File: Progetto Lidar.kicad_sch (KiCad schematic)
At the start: 18 parts, among them IC1 TLV74133PDBVR, J1 CONN_LASER, J2 Conn_Coaxial, Y1 SiT2024BA-S2-33E-8.000000G

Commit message: Finito lo schematico e aggiunto modelli 3D
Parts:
- removed C?: 0.1uF, symbol Device:C
- removed C?: 1uF, symbol Device:C
- added C3, C5, C6: 100nF, Capacitor_SMD:C_0805_2012Metric, symbol Device:C
- added J10, J5, J6, J7, J9: Conn_01x08, Connector_PinSocket_2.54mm:PinSocket_1x08_P2.54mm_Vertical, symbol Connector_Generic:Conn_01x08
- added J3: Conn_02x18_Odd_Even, Connector_PinSocket_2.54mm:PinSocket_2x18_P2.54mm_Vertical, symbol Connector_Generic:Conn_02x18_Odd_Even
- added J4: Conn_01x10, Connector_PinSocket_2.54mm:PinSocket_1x10_P2.54mm_Vertical, symbol Connector_Generic:Conn_01x10
- added J8: Conn_SPI, Connector_PinSocket_2.54mm:PinSocket_2x03_P2.54mm_Vertical, symbol Connector_Generic:Conn_02x03_Odd_Even
- C1: value C -> 0.1uF; footprint (none) -> Capacitor_SMD:C_0805_2012Metric
- C2: value C -> 1uF; footprint (none) -> Capacitor_SMD:C_0805_2012Metric
- C4: renamed from C?; footprint (none) -> Capacitor_SMD:C_0805_2012Metric
- C7: renamed from C?; value 1uF -> 100nF; footprint (none) -> Capacitor_SMD:C_0805_2012Metric
- J1, J2: footprint (none) -> Libreria_componenti_footprint:731713150
- JP1, JP3: renamed from JP?; footprint (none) -> Jumper:SolderJumper-2_P1.3mm_Open_RoundedPad1.0x1.5mm
- JP2: renamed from JP?; footprint (none) -> Jumper:SolderJumper-3_P1.3mm_Open_Pad1.0x1.5mm_NumberLabels
- R1: renamed from R?; footprint (none) -> Resistor_SMD:R_0805_2012Metric
- renumbered IC to IC2
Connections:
- net +3V3: now also C3.1, C5.1, C6.1; no longer IC_1.14 (VDD)
- net +5V: now also A1.5V2 (SPI_5V), A1.5V3 (5V), A1.5V4 (5V), J3.1 (Pin_1), J3.2 (Pin_2), J7.5 (Pin_5), J8.2 (Pin_2)
- net 3V3_ARDUINO: now also J7.4 (Pin_4)
- net ARD_BUFF_EN: now also J5.3 (Pin_3)
- net ARD_TRIG: now also J5.4 (Pin_4)
- net ARD_V_REF: now also J5.5 (Pin_5)
- net GND: now also A1.GND4 (SPI_GND), J1.MH1 (Ext), J2.MH1 (Ext), C5.2, C6.2, J3.35 (Pin_35), J3.36 (Pin_36), J4.4 (Pin_4), J7.6 (Pin_6), J7.7 (Pin_7), J8.6 (Pin_6); no longer J1.2 (Ext), J2.2 (Ext)
- net SPI_CS: now also J5.6 (Pin_6)
- net SPI_MISO: now also J8.1 (Pin_1)
- net SPI_MOSI: now also J8.4 (Pin_4)
- net SPI_SCK: now also J8.3 (Pin_3)
- net at C2.1, IC1.5 (OUT): now also JP2.1 (A)
- net ARD_AN_A0: now reaches A1.A0
- net ARD_AN_A0: now also J9.1 (Pin_1)
- net ARD_AN_A1: now reaches A1.A1
- net ARD_AN_A1: now also J9.2 (Pin_2)
- net ARD_AN_A10: now reaches A1.A10
- net ARD_AN_A10: now also J10.3 (Pin_3)
- net ARD_AN_A11: now reaches A1.A11
- net ARD_AN_A11: now also J10.4 (Pin_4)
- net ARD_AN_A2: now reaches A1.A2
- net ARD_AN_A2: now also J9.3 (Pin_3)
- net ARD_AN_A3: now reaches A1.A3
- net ARD_AN_A3: now also J9.4 (Pin_4)
- net ARD_AN_A4: now reaches A1.A4
- net ARD_AN_A4: now also J9.5 (Pin_5)
- net ARD_AN_A5: now reaches A1.A5
- net ARD_AN_A5: now also J9.6 (Pin_6)
- net ARD_AN_A6: now reaches A1.A6
- net ARD_AN_A6: now also J9.7 (Pin_7)
- net ARD_AN_A7: now reaches A1.A7
- net ARD_AN_A7: now also J9.8 (Pin_8)
- net ARD_AN_A8: now reaches A1.A8
- net ARD_AN_A8: now also J10.1 (Pin_1)
- net ARD_AN_A9: now reaches A1.A9
- net ARD_AN_A9: now also J10.2 (Pin_2)
- net ARD_AN_AREF: now reaches A1.AREF
- net ARD_AN_AREF: now also J4.3 (Pin_3)
- net ARD_CAN_RX: now reaches A1.CANR (CANRX)
- net ARD_CAN_RX: now also J10.7 (Pin_7)
- net ARD_CAN_TX: now reaches A1.CANT (CANTX)
- net ARD_CAN_TX: now also J10.8 (Pin_8)
- net ARD_SR_RX0: now reaches A1.D0 (D0/RX0)
- net ARD_SR_RX0: now also J5.8 (Pin_8)
- net ARD_SR_TX0: now reaches A1.D1 (D1/TX0)
- net ARD_SR_TX0: now also J5.7 (Pin_7)
- net ARD_GPIO_D10: now reaches A1.D10 (D10_CS0)
- net ARD_GPIO_D10: now also J4.8 (Pin_8)
- net ARD_GPIO_D11: now reaches A1.D11
- net ARD_GPIO_D11: now also J4.7 (Pin_7)
- net ARD_GPIO_D12: now reaches A1.D12
- net ARD_GPIO_D12: now also J4.6 (Pin_6)
- net ARD_GPIO_D13: now reaches A1.D13
- net ARD_GPIO_D13: now also J4.5 (Pin_5)
- net ARD_SR_TX3: now reaches A1.D14 (D14/TX3)
- net ARD_SR_TX3: now also J6.1 (Pin_1)
- net ARD_SR_RX3: now reaches A1.D15 (D15/RX3)
- net ARD_SR_RX3: now also J6.2 (Pin_2)
- net ARD_SR_TX2: now reaches A1.D16 (D16/TX2)
- net ARD_SR_TX2: now also J6.3 (Pin_3)
- net ARD_SR_RX2: now reaches A1.D17 (D17/RX2)
- net ARD_SR_RX2: now also J6.4 (Pin_4)
- net ARD_SR_TX1: now reaches A1.D18 (D18/TX1)
- net ARD_SR_TX1: now also J6.5 (Pin_5)
- net ARD_SR_RX1: now reaches A1.D19 (D19/RX1)
- net ARD_SR_RX1: now also J6.6 (Pin_6)
- net ARD_I2C_SDA: now reaches A1.D20 (D20/SDA)
- net ARD_I2C_SDA: now also J6.7 (Pin_7)
- net ARD_I2C_SCL: now reaches A1.D21 (D21/SCL)
- net ARD_I2C_SCL: now also J6.8 (Pin_8)
- net ARD_GPIO_D22: now reaches A1.D22
- net ARD_GPIO_D22: now also J3.3 (Pin_3)
- net ARD_GPIO_D23: now reaches A1.D23
- net ARD_GPIO_D23: now also J3.4 (Pin_4)
- net ARD_GPIO_D24: now reaches A1.D24
- net ARD_GPIO_D24: now also J3.5 (Pin_5)
- net ARD_GPIO_D25: now reaches A1.D25
- net ARD_GPIO_D25: now also J3.6 (Pin_6)
- net ARD_GPIO_D26: now reaches A1.D26
- net ARD_GPIO_D26: now also J3.7 (Pin_7)
- net ARD_GPIO_D27: now reaches A1.D27
- net ARD_GPIO_D27: now also J3.8 (Pin_8)
- net ARD_GPIO_D28: now reaches A1.D28
- net ARD_GPIO_D28: now also J3.9 (Pin_9)
- net ARD_GPIO_D29: now reaches A1.D29
- net ARD_GPIO_D29: now also J3.10 (Pin_10)
- net ARD_GPIO_D30: now reaches A1.D30
- net ARD_GPIO_D30: now also J3.11 (Pin_11)
- net ARD_GPIO_D31: now reaches A1.D31
- net ARD_GPIO_D31: now also J3.12 (Pin_12)
- net ARD_GPIO_D32: now reaches A1.D32
- net ARD_GPIO_D32: now also J3.13 (Pin_13)
- net ARD_GPIO_D33: now reaches A1.D33
- net ARD_GPIO_D33: now also J3.14 (Pin_14)
- net ARD_GPIO_D34: now reaches A1.D34
- net ARD_GPIO_D34: now also J3.15 (Pin_15)
- net ARD_GPIO_D35: now reaches A1.D35
- net ARD_GPIO_D35: now also J3.16 (Pin_16)
- net ARD_GPIO_D36: now reaches A1.D36
- net ARD_GPIO_D36: now also J3.17 (Pin_17)
- net ARD_GPIO_D37: now reaches A1.D37
- net ARD_GPIO_D37: now also J3.18 (Pin_18)
- net ARD_GPIO_D38: now reaches A1.D38
- net ARD_GPIO_D38: now also J3.19 (Pin_19)
- net ARD_GPIO_D39: now reaches A1.D39
- net ARD_GPIO_D39: now also J3.20 (Pin_20)
- net ARD_GPIO_D40: now reaches A1.D40
- net ARD_GPIO_D40: now also J3.21 (Pin_21)
- net ARD_GPIO_D41: now reaches A1.D41
- net ARD_GPIO_D41: now also J3.22 (Pin_22)
- net ARD_GPIO_D42: now reaches A1.D42
- net ARD_GPIO_D42: now also J3.23 (Pin_23)
- net ARD_GPIO_D43: now reaches A1.D43
- net ARD_GPIO_D43: now also J3.24 (Pin_24)
- net ARD_GPIO_D44: now reaches A1.D44
- net ARD_GPIO_D44: now also J3.25 (Pin_25)
- net ARD_GPIO_45: now reaches A1.D45
- net ARD_GPIO_45: now also J3.26 (Pin_26)
- net ARD_GPIO_46: now reaches A1.D46
- net ARD_GPIO_46: now also J3.27 (Pin_27)
- net ARD_GPIO_47: now reaches A1.D47
- net ARD_GPIO_47: now also J3.28 (Pin_28)
- net ARD_GPIO_48: now reaches A1.D48
- net ARD_GPIO_48: now also J3.29 (Pin_29)
- net ARD_GPIO_49: now reaches A1.D49
- net ARD_GPIO_49: now also J3.30 (Pin_30)
- net ARD_GPIO_50: now reaches A1.D50
- net ARD_GPIO_50: now also J3.31 (Pin_31)
- net ARD_GPIO_51: now reaches A1.D51
- net ARD_GPIO_51: now also J3.32 (Pin_32)
- net ARD_GPIO_52: now reaches A1.D52 (D52_CS2)
- net ARD_GPIO_52: now also J3.33 (Pin_33)
- net ARD_GPIO_D53: now reaches A1.D53
- net ARD_GPIO_D53: now also J3.34 (Pin_34)
- net ARD_GPIO_D6: now reaches A1.D6
- net ARD_GPIO_D6: now also J5.2 (Pin_2)
- net ARD_GPIO_D7: now reaches A1.D7
- net ARD_GPIO_D7: now also J5.1 (Pin_1)
- net ARD_GPIO_D8: now reaches A1.D8
- net ARD_GPIO_D8: now also J4.10 (Pin_10)
- net ARD_GPIO_D9: now reaches A1.D9
- net ARD_GPIO_D9: now also J4.9 (Pin_9)
- net ARD_AN_DAC0: now reaches A1.DAC0
- net ARD_AN_DAC0: now also J10.5 (Pin_5)
- net ARD_AN_DAC1: now reaches A1.DAC1
- net ARD_AN_DAC1: now also J10.6 (Pin_6)
- net ARD_AN_IORF: now reaches A1.IORF (IOREF)
- net ARD_AN_IORF: now also J7.2 (Pin_2)
- net ARD_AN_RST1: now reaches A1.RST1 (RESET)
- net ARD_AN_RST1: now also J7.3 (Pin_3)
- net SPI_RESET: now reaches A1.RST2 (SPI_RESET)
- net SPI_RESET: now also J8.5 (Pin_5)
- net ARD_I2C_SCL1: now reaches A1.SCL1
- net ARD_I2C_SCL1: now also J4.1 (Pin_1)
- net ARD_I2C_SDA1: now reaches A1.SDA1
- net ARD_I2C_SDA1: now also J4.2 (Pin_2)
- net ARD_VIN: now reaches A1.VIN
- net ARD_VIN: now also J7.8 (Pin_8)
- new net: C3.2, IC_1.14 (VDD)
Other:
- note added: "Ceramico con ESR: 100 mOhm max"
- moved on the sheet: A1, C1, C2, C4, C7, IC1, IC2, IC_1, IC_2, J1, J2, JP1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

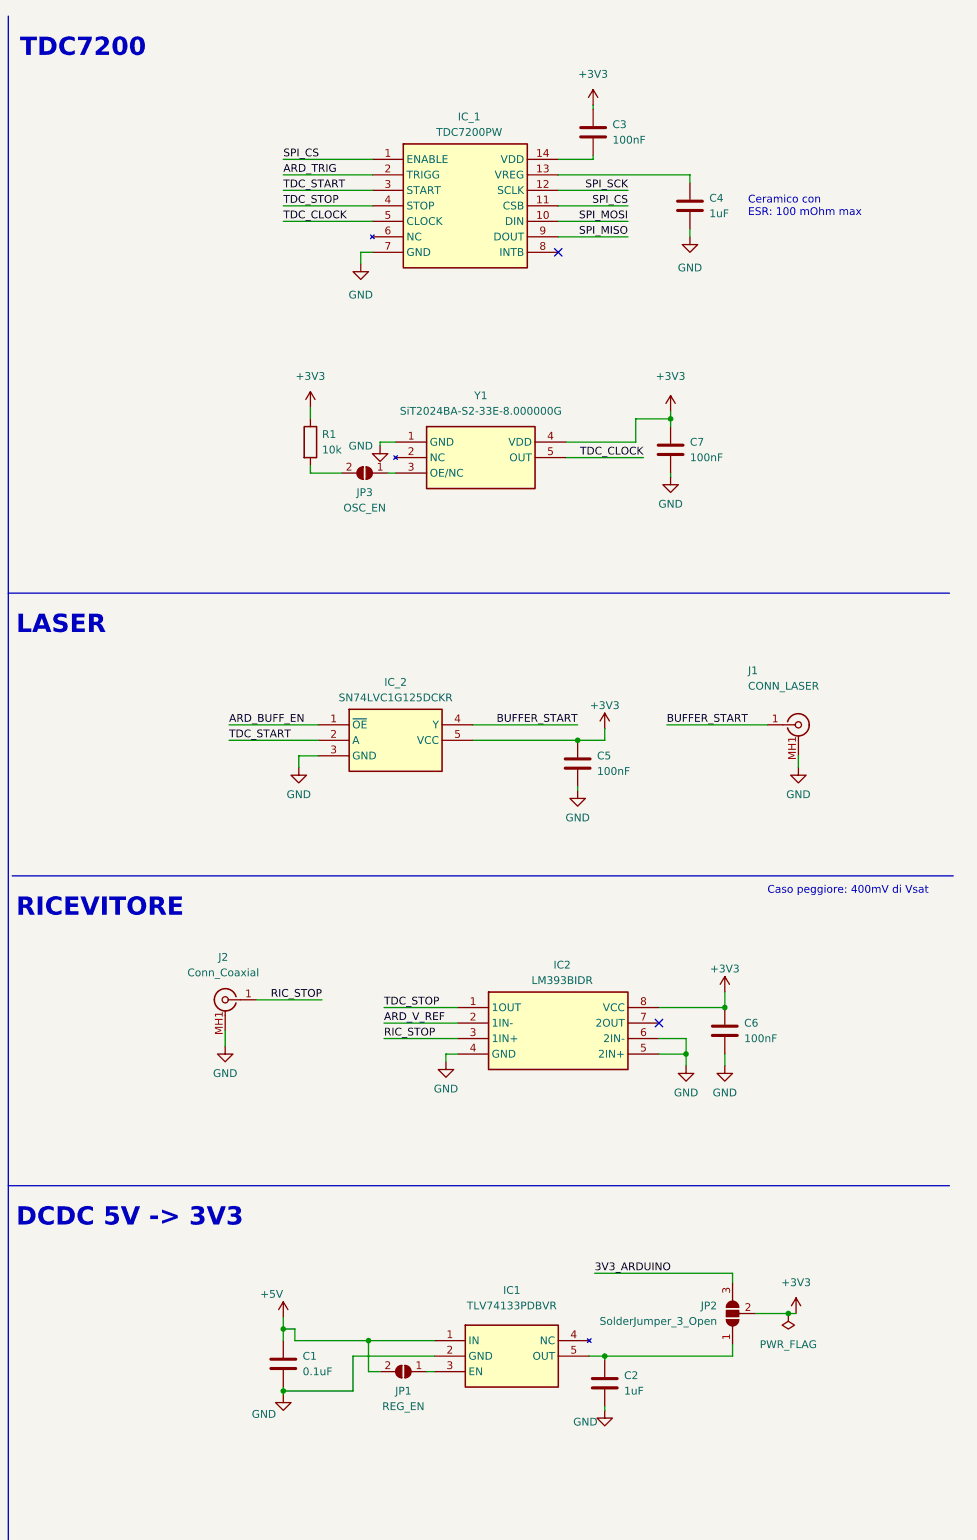
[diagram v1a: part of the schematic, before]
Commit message: Finito il layout della prima versione della scheda
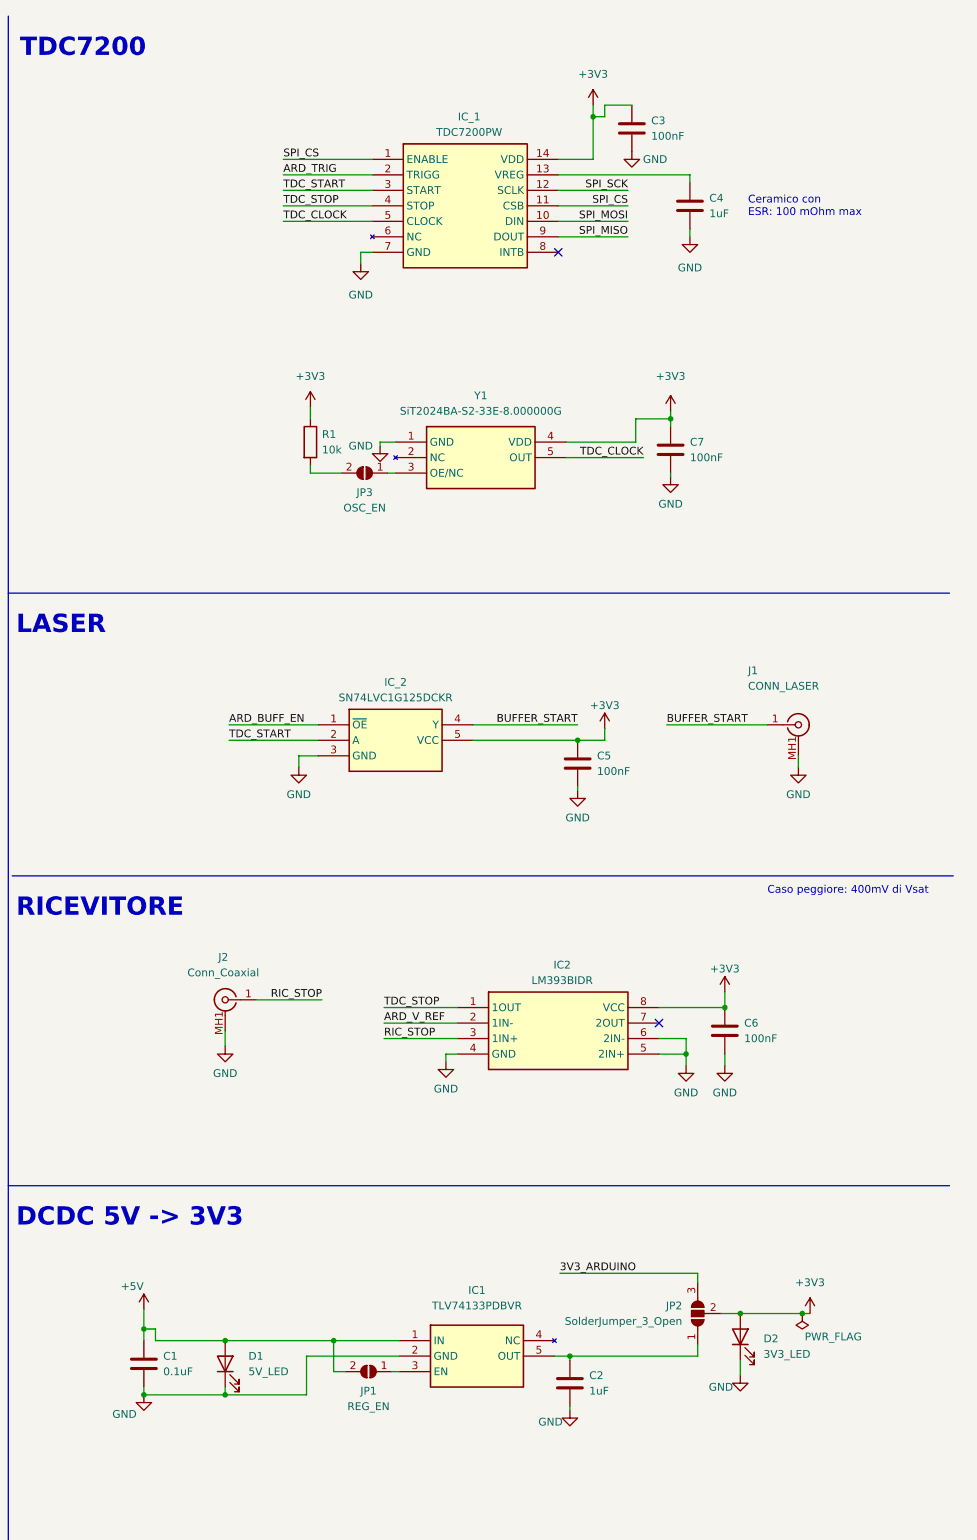
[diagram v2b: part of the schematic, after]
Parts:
- added D1: 5V_LED, LED_SMD:LED_0805_2012Metric, symbol Device:LED
- added D2: 3V3_LED, LED_SMD:LED_0805_2012Metric, symbol Device:LED
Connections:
- net +3V3: now also IC_1.14 (VDD), D2.2 (A)
- net +5V: now also D1.2 (A)
- net GND: now also C3.2, D1.1 (K), D2.1 (K)
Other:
- moved on the sheet: C1, C2, C3, IC1, JP1, JP2

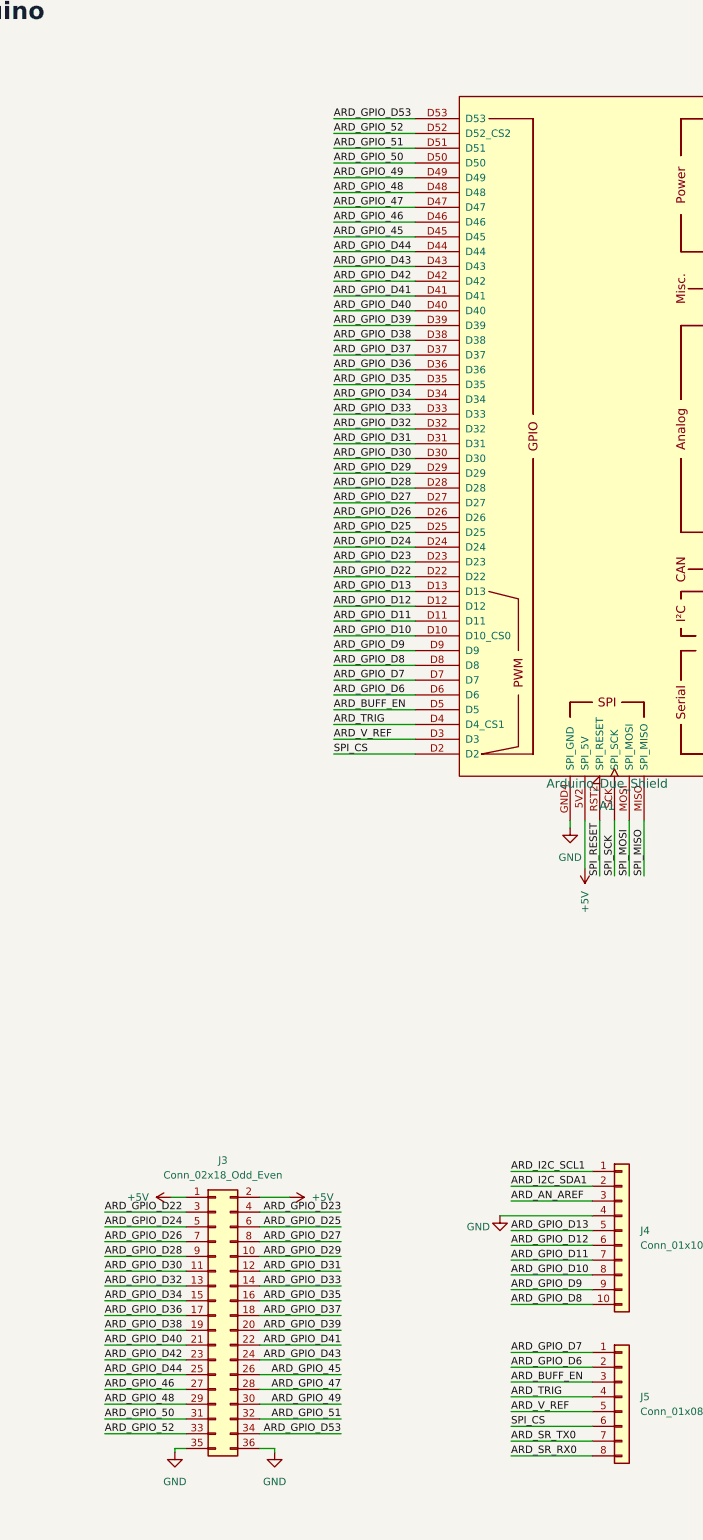
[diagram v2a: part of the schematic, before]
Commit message: Specchiato Arduino per funzionare con connettori femmina
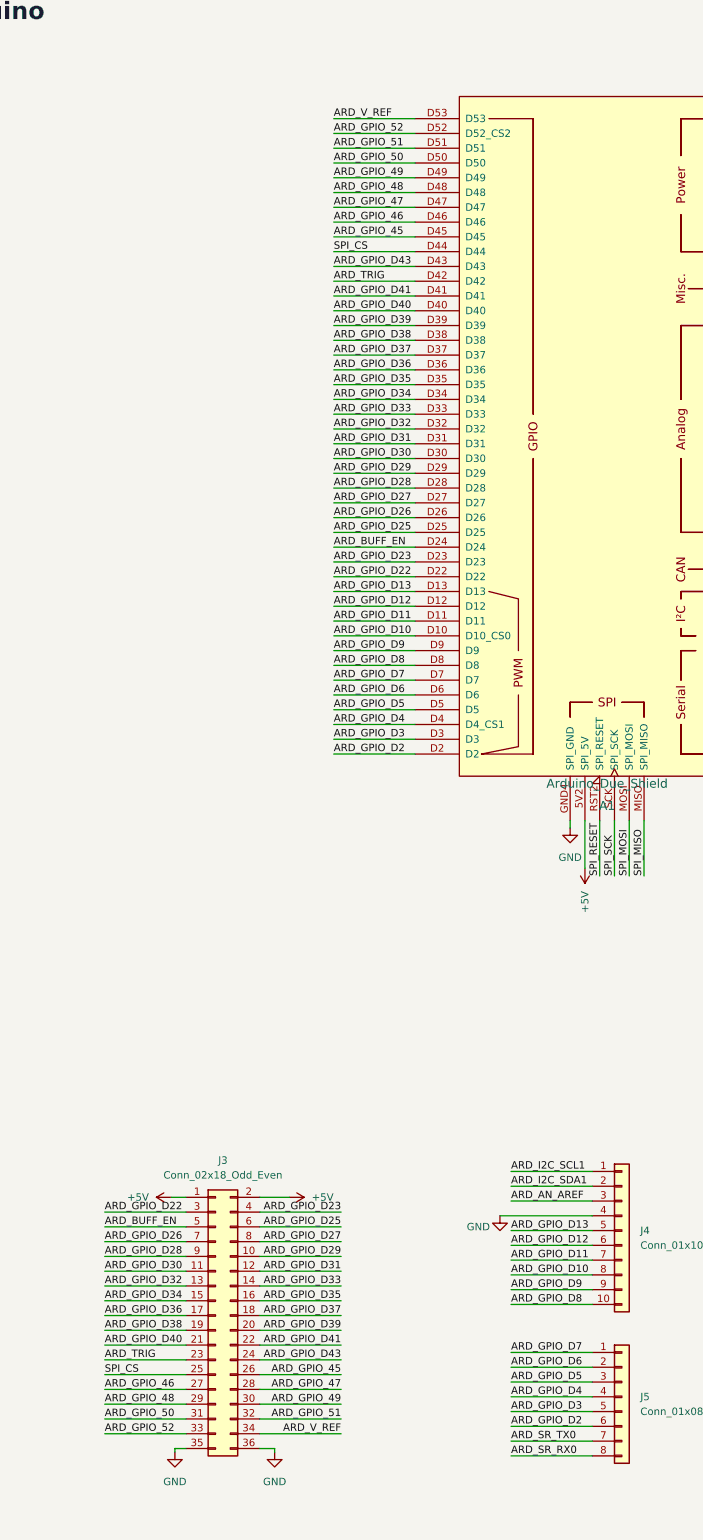
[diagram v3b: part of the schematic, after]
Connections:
- net ARD_GPIO_D24 is gone; now on net ARD_BUFF_EN: A1.D24, J3.5 (Pin_5)
- net ARD_GPIO_D42 is gone; now on net ARD_TRIG: A1.D42, J3.23 (Pin_23)
- net ARD_GPIO_D44 is gone; now on net SPI_CS: A1.D44, J3.25 (Pin_25)
- net ARD_GPIO_D53 is gone; now on net ARD_V_REF: A1.D53, J3.34 (Pin_34)
- net ARD_BUFF_EN: no longer A1.D5, J5.3 (Pin_3)
- net ARD_TRIG: no longer A1.D4 (D4_CS1), J5.4 (Pin_4)
- net ARD_V_REF: no longer A1.D3, J5.5 (Pin_5)
- net SPI_CS: no longer A1.D2, J5.6 (Pin_6)
- new net ARD_GPIO_D2: A1.D2, J5.6 (Pin_6)
- new net ARD_GPIO_D3: A1.D3, J5.5 (Pin_5)
- new net ARD_GPIO_D4: A1.D4 (D4_CS1), J5.4 (Pin_4)
- new net ARD_GPIO_D5: A1.D5, J5.3 (Pin_3)

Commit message: Apportate modifiche dopo incontro con prof. 25.03.2025
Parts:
- removed IC2: LM393BIDR, Libreria_componenti_footprint:SOIC127P600X175-8N, symbol Libreria_componenti:LM393BIDR
- added C8, C9: 1nF, Capacitor_SMD:C_0805_2012Metric, symbol Device:C
- added IC2: LT1719IS6#TRPBF, Libreria_componenti_footprint:SOT95P280X100-6N, symbol Libreria_componenti:LT1719IS6#TRPBF
- added R2: 1k8, Resistor_SMD:R_0805_2012Metric, symbol Device:R
- added R3: 820, Resistor_SMD:R_0805_2012Metric, symbol Device:R
- J1, J2: footprint Libreria_componenti_footprint:731713150 -> Connector_Coaxial:SMA_Molex_73251-1153_EdgeMount_Horizontal
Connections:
- net ARD_AN_DAC0 is gone; now on net ARD_V_REF: A1.DAC0, J10.5 (Pin_5)
- net +3V3: now also C8.1, C9.1, IC2.4 (V+), R3.1; no longer D2.2 (A)
- net +5V: now also R2.1; no longer D1.2 (A)
- net ARD_V_REF: now also IC2.1 (-IN); no longer A1.D53, J3.34 (Pin_34)
- net GND: now also J1.2 (Ext), J2.2 (Ext), C8.2, C9.2, IC2.2 (V-), IC2.6 (SHDN); no longer J1.MH1 (Ext), J2.MH1 (Ext)
- net RIC_STOP: now also IC2.3 (+IN)
- net TDC_STOP: now also IC2.5 (OUT)
- new net: D1.2 (A), R2.2
- new net: D2.2 (A), R3.2
- new net ARD_GPIO_53: A1.D53, J3.34 (Pin_34)
- no-connect marks 3 -> 2
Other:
- note added: "-5V) (5-1.8)/0.002= 1600 -> 1k8 -3V3) (3.3-1.8)/0.002=750 -> 820"
- note added: "LED ROSSI: Vf = 1.8V; If = 2mA"
- note removed: "Caso peggiore: 400mV di Vsat"
- moved on the sheet: C6, J1, J2

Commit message: Finito layout e schematico. Aggiornato Silkscreen
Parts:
- J2: value Conn_Coaxial -> CONN_RICEVITORE
- JP2: value SolderJumper_3_Open -> LDO_EN
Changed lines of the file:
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@@
   (symbol (lib_id "Connector:Conn_Coaxial") (at 277.495 173.355 0) (mirror y) (unit 1)
     (in_bom yes) (on_board yes) (fields_autoplaced)
-    (property "Reference" "J2" (id 0) (at 277.1776 166.37 0))
-    (property "Value" "Conn_Coaxial" (id 1) (at 277.1776 168.91 0))
+    (property "Reference" "J2" (id 0) (at 277.8124 166.37 0))
+    (property "Value" "CONN_RICEVITORE" (id 1) (at 277.8124 168.91 0))
     (property "Footprint" "Connector_Coaxial:SMA_Molex_73251-1153_EdgeMount_Horizontal" (id 2) (at 277.495 173.355 0)
       (effects (font (size 1.27 1.27)) hide)
@@
       (effects (font (size 1.27 1.27)) (justify left))
     )
-    (property "Value" "SolderJumper_3_Open" (id 1) (at 363.855 226.0599 90)
+    (property "Value" "LDO_EN" (id 1) (at 363.855 226.0599 90)
       (effects (font (size 1.27 1.27)) (justify left))
     )
@@
     )
     (path "/91567851-a6e7-4c18-9c1d-beb92ecb179c"
-      (reference "J2") (unit 1) (value "Conn_Coaxial") (footprint "Connector_Coaxial:SMA_Molex_73251-1153_EdgeMount_Horizontal")
+      (reference "J2") (unit 1) (value "CONN_RICEVITORE") (footprint "Connector_Coaxial:SMA_Molex_73251-1153_EdgeMount_Horizontal")
     )
     (path "/eba42262-809f-463f-9f17-44704f171493"
@@
     )
     (path "/daf39426-ed50-4711-8fa2-fa5fc345f9a3"
-      (reference "JP2") (unit 1) (value "SolderJumper_3_Open") (footprint "Jumper:SolderJumper-3_P1.3mm_Open_Pad1.0x1.5mm_NumberLabels")
+      (reference "JP2") (unit 1) (value "LDO_EN") (footprint "Jumper:SolderJumper-3_P1.3mm_Open_Pad1.0x1.5mm_NumberLabels")
     )
     (path "/db1799f5-1bfc-4a07-910b-5e385634249d"
